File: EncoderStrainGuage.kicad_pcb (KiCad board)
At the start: 2 copper layers, 90.6 x 47.7 mm, 76 parts, among them IC1 LM60CIM3_NOPB, J1 Conn_01x05, J2 MM8130-2600RA2, J3 MM8130-2600RA2, J4 Conn_01x12, J7 47219-2001, U1 PIC16LF88-I_SO, U2 OPAMP, U3 CC2570RHAT, U4 AP3428KTTR, U5 MCP6N11T, Y1 Crystal_GND24, Y2 Crystal

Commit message: Fixed RF stuff
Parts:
- removed FL1: LFB182G45BG2D280, LFB182G45BG2D280:LFB182G45BG5D920_1
- removed NP2: ?, Capacitor_SMD:C_0603_1608Metric
- removed U1: PIC16LF88-I_SO, PIC16LF88-I_SO:SOIC127P1030X265-18N
- added C21: 18pF, Capacitor_SMD:C_0603_1608Metric, F.Cu at (132.4, 116.5)
- added C22: 1pF, Capacitor_SMD:C_0603_1608Metric, F.Cu at (130.2, 117.3)
- added C33: 1pF, Capacitor_SMD:C_0603_1608Metric, F.Cu at (128.0, 115.1)
- added C35: .1u, Capacitor_SMD:C_0603_1608Metric, B.Cu at (149.8, 129.5)
- added IC2: PIC16LF1826-I_SO, Package_SO:SOIC-18W_7.5x11.6mm_P1.27mm, F.Cu at (160.5, 128.4)
- added L7: 2nH, Inductor_SMD:L_0603_1608Metric_Pad1.05x0.95mm_HandSolder, F.Cu at (130.2, 114.2)
- added L8: 2nH, Inductor_SMD:L_0603_1608Metric, F.Cu at (128.0, 116.5)
- added L9: 1nH, Inductor_SMD:L_0603_1608Metric_Pad1.05x0.95mm_HandSolder, F.Cu at (124.9, 115.9)
- C1, C10, C13, C16, C17, C18, C29, C30, C5, C6, C7, C8, R10, R11, R12, R13, R2, R7, R8, R9: moved to B.Cu
- C34: renamed from NP4; value ? -> 1pF
- C4: value 100n -> 18pF
- J1: footprint Connector_PinHeader_2.54mm:PinHeader_1x05_P2.54mm_Vertical -> Connector_PinSocket_2.54mm:PinSocket_1x05_P2.54mm_Vertical
- L10: renamed from NP3; value ? -> 3nH
- R5: value 100 -> 1k; moved to B.Cu
- R6: value 100 -> 10k; moved to B.Cu
- moved L6 48.0 mm to (139.9, 133.0), turned to 190 degrees
- moved J7 46.5 mm to (128.1, 129.5), turned to 10 degrees
- moved L5 46.2 mm to (142.9, 129.1), turned to 10 degrees
- moved L4 45.3 mm to (139.3, 128.0), turned to 190 degrees
- moved C31 42.3 mm to (143.3, 132.4), turned to 10 degrees
- moved C30 38.7 mm to (128.2, 135.9), turned to 190 degrees
- moved C32 36.1 mm to (140.0, 134.7), turned to 10 degrees
- moved R1 34.9 mm to (142.7, 127.4), turned to 10 degrees
- moved C17 34.7 mm to (135.4, 114.0), turned to 180 degrees
- moved R17 34.6 mm to (143.3, 130.7), turned to 10 degrees
- moved C4 33.8 mm to (132.4, 115.1), turned to 180 degrees
- moved C29 33.8 mm to (127.9, 134.1), turned to 190 degrees
- moved C18 33.4 mm to (138.4, 111.5), turned to 90 degrees
- moved C28 32.8 mm to (146.1, 128.5), turned to 10 degrees
- moved C27 32.6 mm to (139.8, 131.3), turned to 190 degrees
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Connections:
- C1 pad 1: Str2_3v3 -> +3V3
- C1 pad 2: Str1_Gnd -> GND
- C10 pad 1: Str1_Gnd -> GND
- C10 pad 2: Str2_3v3 -> +3V3
- C11 pad 1: Str1_Gnd -> GND
- C12 pad 2: Str1_Gnd -> GND
- C13 pad 1: Str2_3v3 -> +3V3
- C13 pad 2: Str1_Gnd -> GND
- C14 pad 1: Str1_Gnd -> GND
- C15 pad 2: Str1_Gnd -> GND
- C16 pad 1: Str1_Gnd -> GND
- C16 pad 2: Str2_3v3 -> +3V3
- C17 pad 1: Str1_Gnd -> GND
- C17 pad 2: Str2_3v3 -> +3V3
- C18 pad 1: Str1_Gnd -> GND
- C18 pad 2: Str2_3v3 -> +3V3
- C19 pad 1: Str2_3v3 -> +3V3
- C2 pad 2: Str1_Gnd -> GND
- C20 pad 1: Str2_3v3 -> +3V3
- C20 pad 2: Str1_Gnd -> GND
- C23 pad 1: Str2_3v3 -> +3V3
- C23 pad 2: Str1_Gnd -> GND
- C24 pad 2: Str1_Gnd -> GND
- C25 pad 2: Str1_Gnd -> GND
- C26 pad 2: Str1_Gnd -> GND
- C27 pad 2: Str1_Gnd -> GND
- C28 pad 2: Str1_Gnd -> GND
- C29 pad 1: Str2_3v3 -> +3V3
- C29 pad 2: Str1_Gnd -> GND
- C3 pad 2: Str1_Gnd -> GND
- C30 pad 1: Str2_3v3 -> +3V3
- C30 pad 2: Str1_Gnd -> GND
- C31 pad 2: Str1_Gnd -> GND
- C32 pad 2: Str1_Gnd -> GND
- C34 pad 1: Net-(FL1-Pad1) -> Net-(C34-Pad1)
- C34 pad 2: Str1_Gnd -> GND
- C4 pad 1: Str2_3v3 -> RFpos
- C4 pad 2: Str1_Gnd -> Net-(C33-Pad1)
- C5 pad 1: Str2_3v3 -> +3V3
- C5 pad 2: Str1_Gnd -> GND
- C6 pad 2: Str1_Gnd -> GND
- C7 pad 1: Str1_Gnd -> GND
- C7 pad 2: Str2_3v3 -> +3V3
- C8 pad 2: Str1_Gnd -> GND
- C9 pad 2: Str1_Gnd -> GND
- IC1 pad 1: Str2_3v3 -> +3V3
- IC1 pad 3: Str1_Gnd -> GND
- J1 pad 2: Str2_3v3 -> ICSPCLK
- J1 pad 3: Str1_Gnd -> ICSPDAT
- J1 pad 4: Net-(J1-Pad4) -> +3V3
- J1 pad 5: Net-(J1-Pad5) -> GND
- J2 pad GND1: Str1_Gnd -> GND
- J2 pad GND2: Str1_Gnd -> GND
- J2 pad GND3: Str1_Gnd -> GND
- J2 pad GND4: Str1_Gnd -> GND
- J3 pad GND1: Str1_Gnd -> GND
- J3 pad GND2: Str1_Gnd -> GND
- J3 pad GND3: Str1_Gnd -> GND
- J3 pad GND4: Str1_Gnd -> GND
- J4 pad 10: Str1_Gnd -> GND
- J4 pad 12: Str1_Gnd -> GND
- J4 pad 2: Str2_3v3 -> +3V3
- J4 pad 4: Str1_Gnd -> GND
- J4 pad 5: PSout -> PSin
- J4 pad 6: Str1_Gnd -> GND
- J4 pad 7: Str2_3v3 -> +3V3
- J7 pad 10: Str1_Gnd -> GND
- J7 pad 11: Str1_Gnd -> GND
- J7 pad 12: Str1_Gnd -> GND
- J7 pad 2: SD_CS -> Net-(J7-Pad2)
- J7 pad 4: Str2_3v3 -> +3V3
- J7 pad 6: Str1_Gnd -> GND
- J7 pad 9: Str1_Gnd -> GND
- L10 pad 1: Net-(FL1-Pad1) -> Net-(J3-PadIN)
- L10 pad 2: Net-(J3-PadIN) -> Net-(C34-Pad1)
- NP1 pad 2: Str1_Gnd -> GND
- R10 pad 1: Str2_3v3 -> +3V3
- R11 pad 2: Str1_Gnd -> GND
- R12 pad 1: Str2_3v3 -> +3V3
- R13 pad 1: Str1_Gnd -> GND
- R14 pad 1: Str1_Gnd -> GND
- R14 pad 2: Str2_3v3 -> +3V3
- R15 pad 1: Str2_3v3 -> +3V3
- R2 pad 1: MCLR -> Net-(C35-Pad1)
- R2 pad 2: Str2_3v3 -> +3V3
- R3 pad 2: PSout -> PSin
- R4 pad 1: Str1_Gnd -> GND
- R5 pad 1: Net-(J1-Pad4) -> MCLR
- R5 pad 2: PGD -> Net-(C35-Pad1)
- R6 pad 1: Net-(J1-Pad5) -> Net-(J7-Pad2)
- R6 pad 2: PGC -> GND
- R7 pad 2: Str1_Gnd -> GND
- R8 pad 1: Str2_3v3 -> +3V3
- R9 pad 2: Str1_Gnd -> GND
- RV1 pad 1: Str1_Gnd -> GND
- RV1 pad 2: Net-(RV1-Pad2) -> Str-
- RV1 pad 3: Str- -> Net-(RV1-Pad3)
- RV2 pad 1: Str- -> Net-(RV2-Pad1)
- RV2 pad 2: Net-(RV2-Pad2) -> Str-
- RV2 pad 3: Str2_3v3 -> +3V3
- RV3 pad 1: Str1_Gnd -> GND
- U2 pad 1: PSout -> PSin
- U2 pad 2: Str1_Gnd -> GND
- U2 pad 4: Str2_3v3 -> +3V3
- U2 pad 5: Str1_Gnd -> GND
- U3 pad 1: Str1_Gnd -> GND
- U3 pad 10: Str2_3v3 -> +3V3
- U3 pad 13: Str1_Gnd -> GND
- U3 pad 17: Str1_Gnd -> GND
- U3 pad 19: Suspend -> +3V3
- U3 pad 2: Str1_Gnd -> GND
- U3 pad 21: Str2_3v3 -> +3V3
- U3 pad 24: Str2_3v3 -> +3V3
- U3 pad 27: Str2_3v3 -> +3V3
- U3 pad 28: Str2_3v3 -> +3V3
- U3 pad 29: Str2_3v3 -> +3V3
- U3 pad 3: Str1_Gnd -> GND
- U3 pad 31: Str2_3v3 -> +3V3
- U3 pad 35: Str1_Gnd -> GND
- U3 pad 37: Str1_Gnd -> GND
- U3 pad 38: Str1_Gnd -> GND
- U3 pad 39: Str2_3v3 -> +3V3
- U3 pad 4: Str1_Gnd -> GND
- U3 pad 41: Str1_Gnd -> GND
- U4 pad 2: Str1_Gnd -> GND
- U4 pad 5: Str2_3v3 -> +3V3
- U5 pad 4: Str1_Gnd -> GND
- U5 pad 5: Str1_Gnd -> GND
- U5 pad 7: Str2_3v3 -> +3V3
- U5 pad 8: Str2_3v3 -> +3V3
- Y1 pad 2: Str1_Gnd -> GND
- Y1 pad 4: Str1_Gnd -> GND
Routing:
- net +3V3: track 0.00 -> 198.8 mm, vias 0 -> 17
- net Str2_3v3: track 173.2 -> 0.00 mm, vias 16 -> 0
- net Str1_Gnd: track 96.2 -> 0.00 mm, vias 11 -> 0
- net GND: track 0.11 -> 54.1 mm, vias 37 -> 159
- net PotOut: track 0.00 -> 39.6 mm, vias 0 -> 2
- net SSTB: track 0.00 -> 35.8 mm, vias 0 -> 2
- net Str+: track 0.00 -> 33.4 mm
- net MISO: track 0.00 -> 27.7 mm, vias 0 -> 2
- net PSout: track 10.0 -> 36.1 mm, vias 0 -> 2
- net Suspend: track 21.6 -> 0.00 mm, vias 2 -> 0
- net MOSI: track 0.00 -> 19.6 mm, vias 0 -> 2
- net UARTrx: track 10.4 -> 29.2 mm, vias 0 -> 2
- net UARTtx: track 19.6 -> 37.0 mm, vias 0 -> 2
- net MCLR: track 11.8 -> 28.7 mm, vias 0 -> 3
- net Reset: track 23.8 -> 40.6 mm, vias 2 -> 4
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- added copper zone on B.Cu, net GND
- added copper zone on F.Cu, net GND
- removed copper zone on B.Cu, net Str1_Gnd
- removed copper zone on F.Cu, net Str1_Gnd

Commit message: Fixed trimmer
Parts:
- moved RV3 0.39 mm to (145.0, 136.2), turned to 225 degrees
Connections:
- RV3 pad 1: GND -> Net-(RV3-Pad1)
- RV3 pad 2: Net-(RV3-Pad2) -> Net-(R18-Pad2)
- RV3 pad 3: Net-(R18-Pad2) -> GND
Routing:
- net Net-(R18-Pad2): track 3.88 -> 5.16 mm
- net GND: vias 159 -> 160
- net (no net): vias 2 -> 1

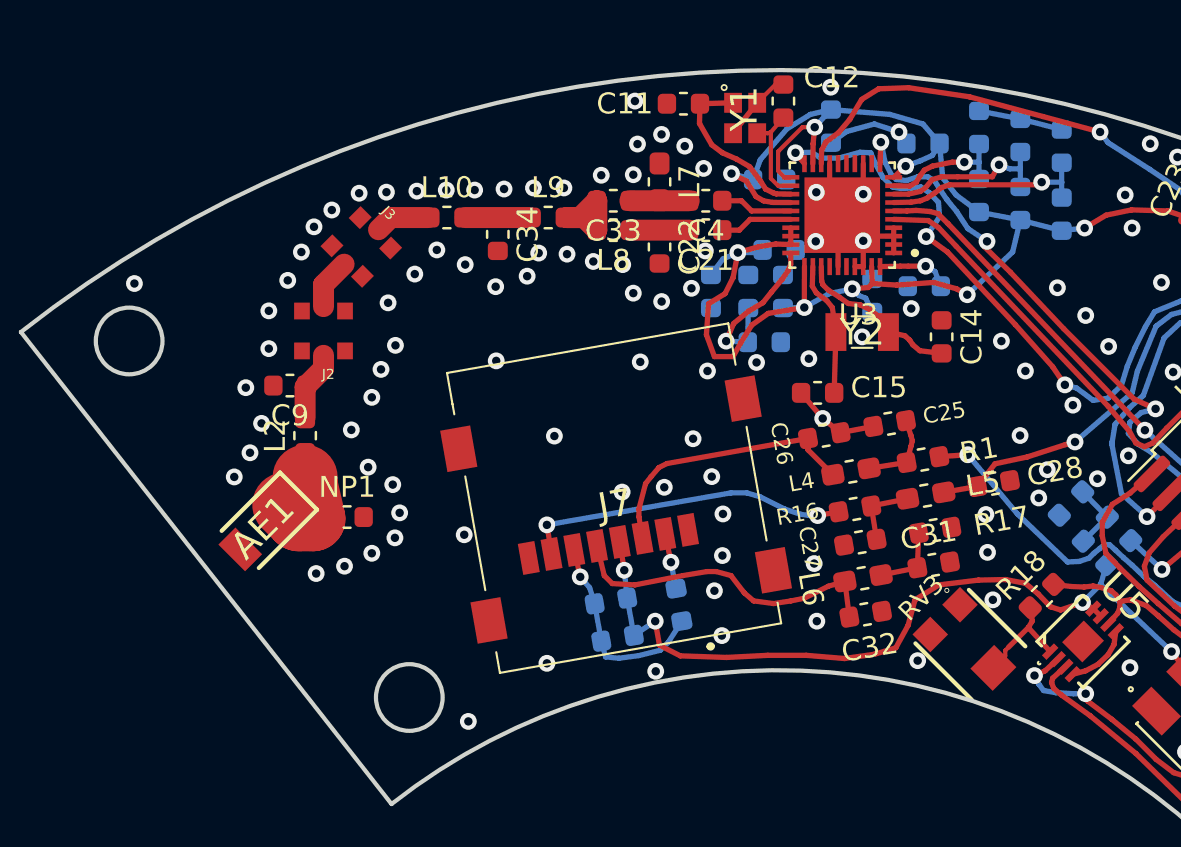
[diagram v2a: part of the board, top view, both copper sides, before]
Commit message: Improved RF routing
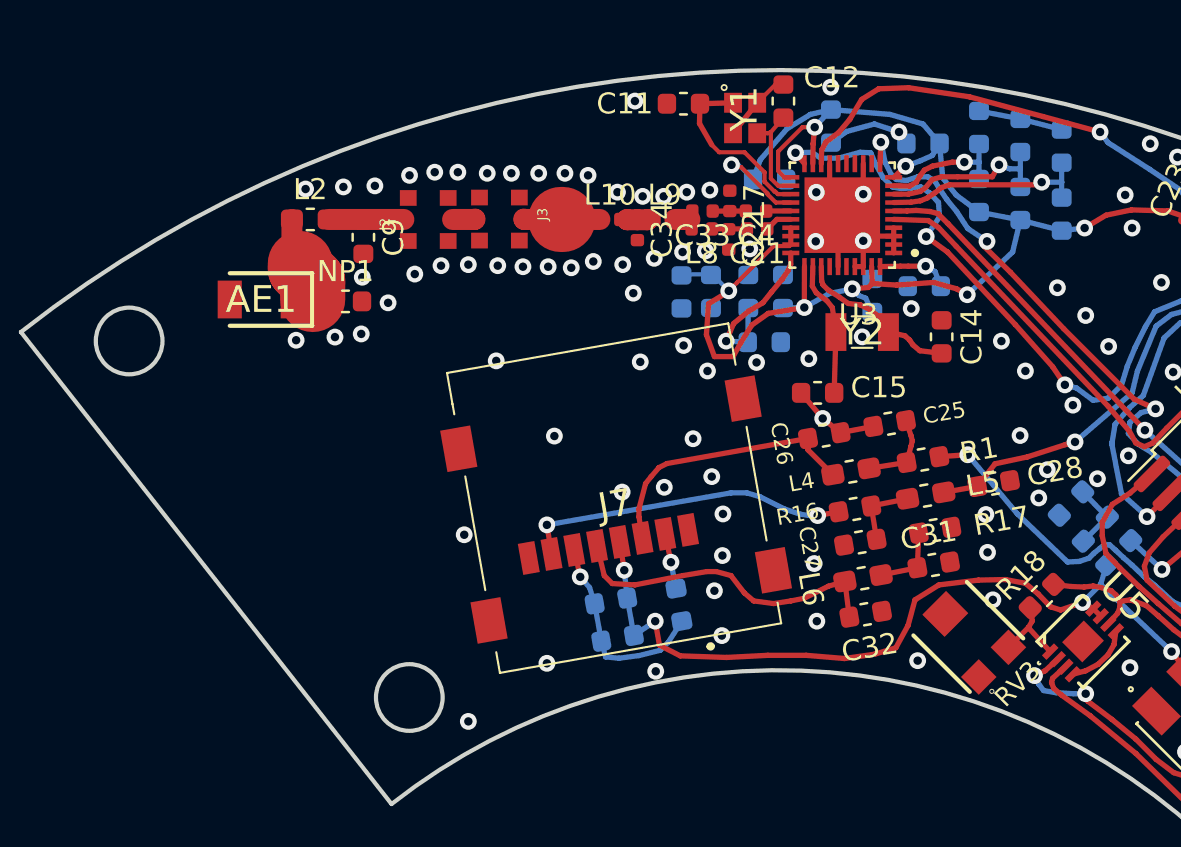
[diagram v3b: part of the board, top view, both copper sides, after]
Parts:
- C21, C22, C33, C34, C4: footprint Capacitor_SMD:C_0603_1608Metric -> Capacitor_SMD:C_0402_1005Metric
- L10, L7, L9: footprint Inductor_SMD:L_0603_1608Metric_Pad1.05x0.95mm_HandSolder -> Inductor_SMD:L_0402_1005Metric
- L8: footprint Inductor_SMD:L_0603_1608Metric -> Inductor_SMD:L_0402_1005Metric
- moved AE1 10.8 mm to (111.2, 119.8), turned to 180 degrees
- moved L2 10.3 mm to (113.6, 116.0), turned to 0 degrees
- moved NP1 10.3 mm to (115.2, 119.8)
- moved C9 7.88 mm to (116.1, 116.8), turned to 270 degrees
- moved L10 7.77 mm to (127.8, 116.0)
- moved J2 7.28 mm to (119.2, 116.0), turned to 90 degrees
- moved J3 6.71 mm to (122.6, 115.9), turned to 270 degrees
- moved C34 6.65 mm to (129.2, 116.5)
- moved L9 5.55 mm to (130.4, 116.0)
- moved C13 5.06 mm to (131.2, 119.4), turned to 270 degrees
- moved C33 4.27 mm to (132.2, 115.5)
- moved L8 4.21 mm to (132.2, 116.4)
- moved L7 3.47 mm to (133.6, 115.1)
- moved C22 3.32 mm to (133.5, 116.9)
- moved C21 2.45 mm to (134.8, 116.4)
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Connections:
- RV3 pad 1: Net-(RV3-Pad1) -> GND
- RV3 pad 2: Net-(R18-Pad2) -> Net-(RV3-Pad2)
- RV3 pad 3: GND -> Net-(R18-Pad2)
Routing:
- net Net-(AE1-Pad1): track 4.74 -> 7.54 mm
- net RFpos: track 3.46 -> 1.26 mm
- net RFneg: track 3.48 -> 1.31 mm
- net Net-(J2-PadOUT): track 2.43 -> 1.08 mm
- net Net-(R18-Pad2): track 5.16 -> 3.88 mm
- net Net-(C33-Pad2): track 4.85 -> 3.59 mm
- net Net-(C33-Pad1): track 2.82 -> 1.58 mm
- net Net-(C21-Pad2): track 2.82 -> 1.67 mm
- net Net-(J3-PadIN): track 2.62 -> 3.73 mm
- net +3V3: track 198.8 -> 197.8 mm
- net GND: vias 160 -> 145
- net (no net): vias 1 -> 2

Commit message: Fixed DRC
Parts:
- moved C20 1.47 mm to (160.3, 139.2), turned to 315 degrees
- moved R15 0.36 mm to (162.5, 137.4)
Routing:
- net Reset: track 40.6 -> 38.1 mm
- net GND: track 54.1 -> 53.0 mm, vias 145 -> 144
- net PotOut: track 39.6 -> 40.2 mm
- net (no net): vias 2 -> 1
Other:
- net class Default: clearance 0.1 -> 0.127
- rule trace_clearance: 0.1 -> 0.127
- rule trace_min: 0.2 -> 0
- rule via_min_size: 0.4 -> 0

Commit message: Fixed some slightly questionable routing
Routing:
- net GND: track 53.0 -> 57.7 mm, vias 144 -> 156
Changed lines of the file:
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@@
     (thickness 1.6)
     (drawings 10)
-    (tracks 910)
+    (tracks 925)
     (zones 0)
     (modules 81)
@@
   )
   (setup
-    (last_trace_width 0.2)
+    (last_trace_width 0.25)
     (user_trace_width 0.2)
     (user_trace_width 0.254)
@@
   (via (at 145.8214 131.8006) (size 0.8) (drill 0.4) (layers F.Cu B.Cu) (net 60))
   (via (at 146.0754 134.0612) (size 0.8) (drill 0.4) (layers F.Cu B.Cu) (net 60))
-  (via (at 130.5 137.15) (size 0.8) (drill 0.4) (layers F.Cu B.Cu) (net 60))
+  (via (at 129.8 137.15) (size 0.8) (drill 0.4) (layers F.Cu B.Cu) (net 60))
   (via (at 133.1722 135.763) (size 0.8) (drill 0.4) (layers F.Cu B.Cu) (net 60))
   (via (at 131.8006 126.3904) (size 0.8) (drill 0.4) (layers F.Cu B.Cu) (net 60))
@@
   (via (at 115.15 114.4) (size 0.8) (drill 0.4) (layers F.Cu B.Cu) (net 60))
   (via (at 113.35 114.5) (size 0.8) (drill 0.4) (layers F.Cu B.Cu) (net 60))
+  (segment (start 152.3746 114.2186) (end 152.3746 114.7826) (width 0.25) (layer B.Cu) (net 60))
+  (segment (start 149.827 111.671) (end 152.3746 114.2186) (width 0.25) (layer B.Cu) (net 60))
+  (segment (start 149.352 111.671) (end 149.827 111.671) (width 0.25) (layer B.Cu) (net 60))
+  (via (at 143.85 110.9) (size 0.8) (drill 0.4) (layers F.Cu B.Cu) (net 60))
+  (via (at 113.9 136.5) (size 0.8) (drill 0.4) (layers F.Cu B.Cu) (net 60))
+  (via (at 113.85 134.05) (size 0.8) (drill 0.4) (layers F.Cu B.Cu) (net 60))
+  (via (at 113.95 131.95) (size 0.8) (drill 0.4) (layers F.Cu B.Cu) (net 60))
+  (via (at 114.1 129.3) (size 0.8) (drill 0.4) (layers F.Cu B.Cu) (net 60))
+  (via (at 114.2 126.85) (size 0.8) (drill 0.4) (layers F.Cu B.Cu) (net 60))
+  (via (at 114.2 124.25) (size 0.8) (drill 0.4) (layers F.Cu B.Cu) (net 60))
+  (via (at 117 124.3) (size 0.8) (drill 0.4) (layers F.Cu B.Cu) (net 60))
+  (via (at 117.65 129.25) (size 0.8) (drill 0.4) (layers F.Cu B.Cu) (net 60))
+  (via (at 116.45 135.45) (size 0.8) (drill 0.4) (layers F.Cu B.Cu) (net 60))
+  (via (at 118.3 132.65) (size 0.8) (drill 0.4) (layers F.Cu B.Cu) (net 60))
+  (via (at 119.35 121.85) (size 0.8) (drill 0.4) (layers F.Cu B.Cu) (net 60))
   (segment (start 136.4538 117.1441) (end 136.4538 116.7441) (width 0.25) (layer F.Cu) (net 61))
   (segment (start 136.4538 116.3441) (end 136.4538 116.7441) (width 0.25) (layer F.Cu) (net 61))
